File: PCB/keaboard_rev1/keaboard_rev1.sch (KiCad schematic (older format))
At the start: 54 parts, among them K01 KEYSW, K02 KEYSW, K03 KEYSW, K04 KEYSW, K05 KEYSW, K06 KEYSW, K07 KEYSW, K08 KEYSW, K09 KEYSW, K10 KEYSW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

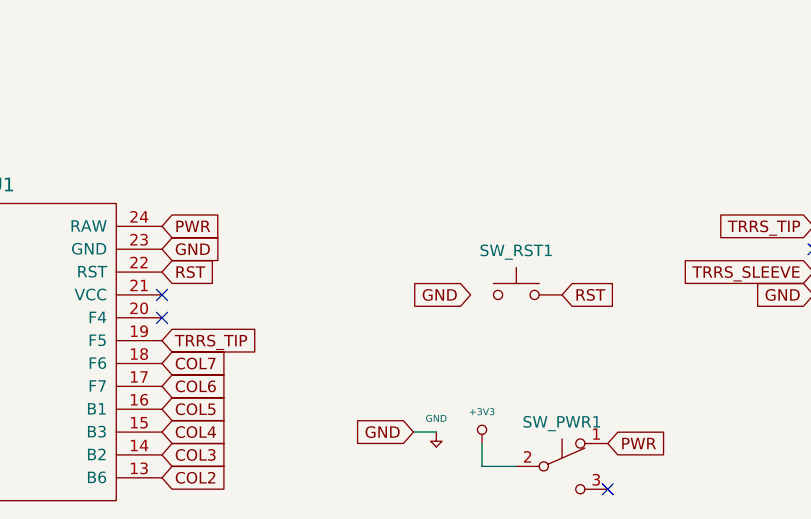
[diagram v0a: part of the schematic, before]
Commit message: Fix reset switch, wire reset switch, wire grounds
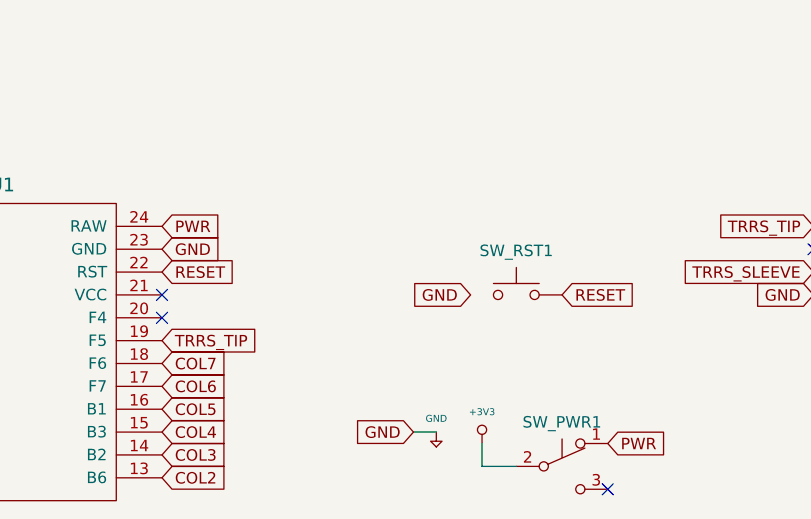
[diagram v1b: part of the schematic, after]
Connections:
- net RST renamed RESET
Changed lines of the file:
@@
 GND
 Text GLabel 2850 6000 2    50   Input ~ 0
-RST
+RESET
 Text GLabel 2850 5800 2    50   Input ~ 0
 PWR
 Text GLabel 4600 6100 2    50   Input ~ 0
-RST
+RESET
 $Comp
 L Switch:SW_Push_SPDT SW_PWR1

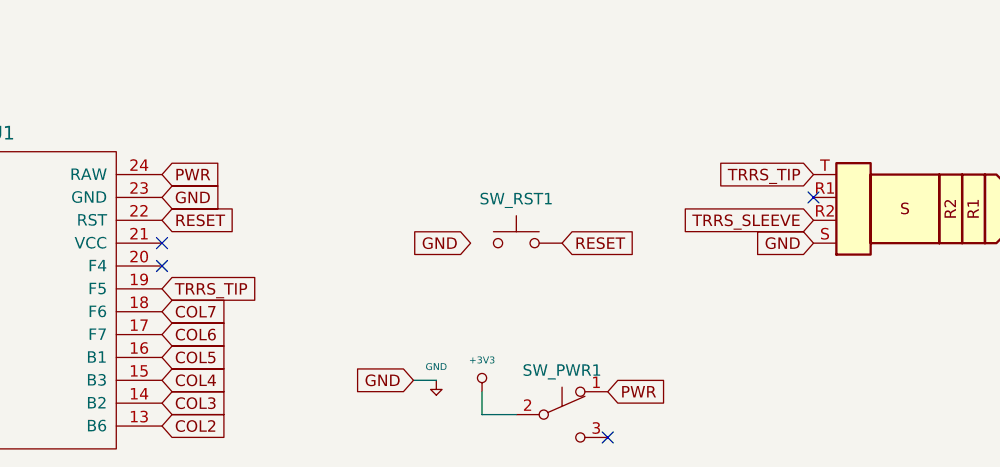
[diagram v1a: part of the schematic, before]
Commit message: Connect battery, fix unconnected lines
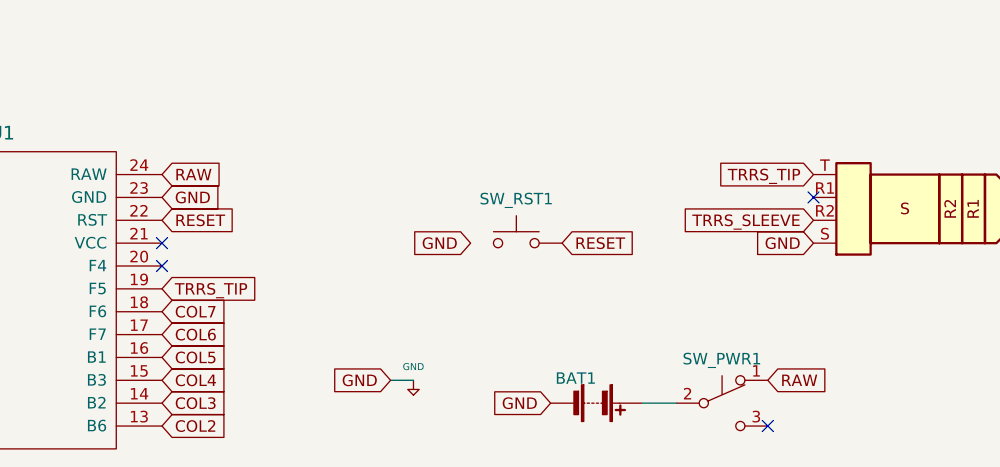
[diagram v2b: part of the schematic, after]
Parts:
- added BAT1: Battery, parts:DF3A-3P-2DS, symbol Device:Battery
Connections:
- net +5V: now also BAT1.2 (-); no longer SW_PWR1.2 (B)
- net PWR renamed RAW
- new net: BAT1.1 (+), SW_PWR1.2 (B)
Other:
- moved on the sheet: SW_PWR1
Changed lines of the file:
@@
 RESET
 Text GLabel 2850 5800 2    50   Input ~ 0
-PWR
+RAW
 Text GLabel 4600 6100 2    50   Input ~ 0
 RESET
@@
 L Switch:SW_Push_SPDT SW_PWR1
 U 1 1 5F83E72F
-P 4600 6850
-F 0 "SW_PWR1" H 4600 7043 50  0000 C CNN
-F 1 "SW_Push_SPDT" H 4600 7044 50  0001 C CNN
-F 2 "parts:SW_PCM12SMTR_reversible" H 4600 6850 50  0001 C CNN
-F 3 "~" H 4600 6850 50  0001 C CNN
-	1    4600 6850
-	1    0    0    -1
-$EndComp
-$Comp
-L keyboard_parts:+3V3 #PWR0101
-U 1 1 5F845A34
-P 4250 6750
-F 0 "#PWR0101" H 4250 6720 20  0001 C CNN
-F 1 "+3V3" H 4250 6888 30  0000 C CNN
-F 2 "parts:DF3A-3P-2DS" H 4250 6750 60  0001 C CNN
-F 3 "" H 4250 6750 60  0001 C CNN
-	1    4250 6750
+P 5300 6800
+F 0 "SW_PWR1" H 5300 6993 50  0000 C CNN
+F 1 "SW_Push_SPDT" H 5300 6994 50  0001 C CNN
+F 2 "parts:SW_PCM12SMTR_reversible" H 5300 6800 50  0001 C CNN
+F 3 "~" H 5300 6800 50  0001 C CNN
+	1    5300 6800
 	1    0    0    -1
 $EndComp
 Wire Wire Line
-	4250 6750 4250 6850
-Wire Wire Line
-	4250 6850 4400 6850
-Text GLabel 4800 6750 2    50   Input ~ 0
-PWR
-NoConn ~ 4800 6950
+	4950 6800 5100 6800
+Text GLabel 5500 6700 2    50   Input ~ 0
+RAW
+NoConn ~ 5500 6900
 NoConn ~ 1450 5800
 NoConn ~ 1450 5900
@@
 NoConn ~ 2850 6200
 NoConn ~ 2850 6100
-Text GLabel 3950 6700 0    50   Input ~ 0
+Text GLabel 3850 6700 0    50   Input ~ 0
 GND
 $Comp
 L keyboard_parts:GND #PWR0102
 U 1 1 5F984A64
-P 4050 6700
-F 0 "#PWR0102" H 4050 6750 20  0001 C CNN
-F 1 "GND" H 4050 6759 30  0000 C CNN
-F 2 "" H 4050 6700 60  0000 C CNN
-F 3 "" H 4050 6700 60  0000 C CNN
-	1    4050 6700
+P 3950 6700
+F 0 "#PWR0102" H 3950 6750 20  0001 C CNN
+F 1 "GND" H 3950 6759 30  0000 C CNN
+F 2 "" H 3950 6700 60  0000 C CNN
+F 3 "" H 3950 6700 60  0000 C CNN
+	1    3950 6700
 	1    0    0    -1
 $EndComp
 Wire Wire Line
-	3950 6700 4050 6700
+	3850 6700 3950 6700
 $Comp
 L Connector:AudioPlug4 TRRS1
@@
 Text GLabel 1450 6100 0    50   Input ~ 0
 GND
+Text GLabel 4550 6800 0    50   Input ~ 0
+GND
+$Comp
+L Device:Battery BAT1
+U 1 1 5FB5DEFC
+P 4750 6800
+F 0 "BAT1" V 4642 6800 50  0000 R CNN
+F 1 "Battery" H 4642 6845 50  0001 R CNN
+F 2 "parts:DF3A-3P-2DS" V 4750 6860 50  0001 C CNN
+F 3 "~" V 4750 6860 50  0001 C CNN
+	1    4750 6800
+	0    1    1    0
+$EndComp
 $EndSCHEMATC

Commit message: Update pcb image, generate gerber
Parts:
- BAT1: footprint parts:DF3A-3P-2DS -> parts:DF3A-3P-2DS_reversible
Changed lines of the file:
@@
 F 0 "BAT1" V 4642 6800 50  0000 R CNN
 F 1 "Battery" H 4642 6845 50  0001 R CNN
-F 2 "parts:DF3A-3P-2DS" V 4750 6860 50  0001 C CNN
+F 2 "parts:DF3A-3P-2DS_reversible" V 4750 6860 50  0001 C CNN
 F 3 "~" V 4750 6860 50  0001 C CNN
 	1    4750 6800

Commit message: Update schematic, update footprints, start updating layout
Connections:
- net COL1: now also U1.19 (F5); no longer U1.12 (B5)
- net COL2: now also U1.18 (F6); no longer U1.13 (B6)
- net COL3: now also U1.17 (F7); no longer U1.14 (B2)
- net COL4: now also U1.16 (B1); no longer U1.15 (B3)
- net COL5: now also U1.15 (B3); no longer U1.16 (B1)
- net COL6: now also U1.14 (B2); no longer U1.17 (F7)
- net COL7: now also U1.13 (B6); no longer U1.18 (F6)
- net ROW1: now also U1.9 (D7); no longer U1.8 (C6)
- net ROW2: now also U1.10 (E6); no longer U1.9 (D7)
- net ROW3: now also U1.11 (B4); no longer U1.10 (E6)
- net ROW4: now also U1.12 (B5); no longer U1.11 (B4)
- net SOFT_SERIAL_PIN: now reaches U1.20 (F4)
- net SOFT_SERIAL_PIN: now also TRRS1.T
- net VCC: now reaches U1.21 (VCC)
- net VCC: now also TRRS1.R2
- net TRRS_SLEEVE: no longer names the net of U1.5 (SCL)
- net TRRS_SLEEVE: no longer TRRS1.R2
- removed net TRRS_TIP: TRRS1.T, U1.19 (F5)
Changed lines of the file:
@@
 	1    0    0    -1
 $EndComp
+Text GLabel 2850 6900 2    50   Input ~ 0
+COL7
+Text GLabel 2850 6300 2    50   Input ~ 0
+COL1
 Text GLabel 2850 6400 2    50   Input ~ 0
-COL7
+COL2
+Text GLabel 2850 6500 2    50   Input ~ 0
+COL3
+Text GLabel 2850 6600 2    50   Input ~ 0
+COL4
+Text GLabel 2850 6700 2    50   Input ~ 0
+COL5
+Text GLabel 2850 6800 2    50   Input ~ 0
+COL6
+Text GLabel 1450 6800 0    50   Input ~ 0
+ROW3
+Text GLabel 1450 6700 0    50   Input ~ 0
+ROW2
+Text GLabel 1450 6600 0    50   Input ~ 0
+ROW1
 Text GLabel 1450 6900 0    50   Input ~ 0
-COL1
-Text GLabel 2850 6900 2    50   Input ~ 0
-COL2
-Text GLabel 2850 6800 2    50   Input ~ 0
-COL3
-Text GLabel 2850 6700 2    50   Input ~ 0
-COL4
-Text GLabel 2850 6600 2    50   Input ~ 0
-COL5
-Text GLabel 2850 6500 2    50   Input ~ 0
-COL6
-Text GLabel 1450 6700 0    50   Input ~ 0
-ROW3
-Text GLabel 1450 6600 0    50   Input ~ 0
-ROW2
-Text GLabel 1450 6500 0    50   Input ~ 0
-ROW1
-Text GLabel 1450 6800 0    50   Input ~ 0
 ROW4
 Wire Wire Line
@@
 NoConn ~ 1450 6300
 NoConn ~ 1450 6400
-NoConn ~ 2850 6200
-NoConn ~ 2850 6100
 Text GLabel 3850 6700 0    50   Input ~ 0
 GND
@@
 	-1   0    0    1
 $EndComp
-Text GLabel 2850 6300 2    50   Input ~ 0
-TRRS_TIP
+Text GLabel 2850 6200 2    50   Input ~ 0
+SOFT_SERIAL_PIN
 Text GLabel 5700 5800 0    50   Input ~ 0
-TRRS_TIP
+SOFT_SERIAL_PIN
 Text GLabel 5700 6000 0    50   Input ~ 0
-TRRS_SLEEVE
-Text GLabel 1450 6200 0    50   Input ~ 0
-TRRS_SLEEVE
+VCC
+Text GLabel 2850 6100 2    50   Input ~ 0
+VCC
 NoConn ~ 5700 5900
 Text GLabel 5700 6100 0    50   Input ~ 0
@@
 	0    1    1    0
 $EndComp
+NoConn ~ 1450 6200
+NoConn ~ 1450 6500
 $EndSCHEMATC

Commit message: Update schematic, TODO: Update pcb
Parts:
- TRRS1: symbol Connector:AudioPlug4 -> keaboard_rev1-rescue:AudioPlug4-Connector
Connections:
- net SOFT_SERIAL_PIN: now also U1.6 (SDA); no longer U1.20 (F4)
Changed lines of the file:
@@
 Text GLabel 8550 950  1    50   Input ~ 0
 COL6
-$Comp
-L promicro:ProMicro U1
-U 1 1 5F595947
-P 2150 6550
-F 0 "U1" H 2150 7481 60  0000 C CNN
-F 1 "ProMicro" H 2150 7481 60  0001 C CNN
-F 2 "parts:ArduinoProMicro_Reversible" H 2150 7481 60  0001 C CNN
-F 3 "" H 2250 5500 60  0000 C CNN
-	1    2150 6550
-	1    0    0    -1
-$EndComp
 Text GLabel 2850 6900 2    50   Input ~ 0
 COL7
@@
 NoConn ~ 1450 5800
 NoConn ~ 1450 5900
-NoConn ~ 1450 6300
-NoConn ~ 1450 6400
 Text GLabel 3850 6700 0    50   Input ~ 0
 GND
@@
 	3850 6700 3950 6700
 $Comp
-L Connector:AudioPlug4 TRRS1
+L keaboard_rev1-rescue:AudioPlug4-Connector TRRS1
 U 1 1 5F9D9D98
 P 6300 6000
@@
 	-1   0    0    1
 $EndComp
-Text GLabel 2850 6200 2    50   Input ~ 0
+Text GLabel 1450 6300 0    50   Input ~ 0
 SOFT_SERIAL_PIN
 Text GLabel 5700 5800 0    50   Input ~ 0
@@
 NoConn ~ 1450 6200
 NoConn ~ 1450 6500
+NoConn ~ 2850 6200
+$Comp
+L promicro:ProMicro U1
+U 1 1 5F595947
+P 2150 6550
+F 0 "U1" H 2150 7481 60  0000 C CNN
+F 1 "ProMicro" H 2150 7481 60  0001 C CNN
+F 2 "parts:ArduinoProMicro_Reversible" H 2150 7481 60  0001 C CNN
+F 3 "" H 2250 5500 60  0000 C CNN
+	1    2150 6550
+	1    0    0    -1
+$EndComp
+NoConn ~ 1450 6400
 $EndSCHEMATC
